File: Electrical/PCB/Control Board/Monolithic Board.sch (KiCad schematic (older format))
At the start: 88 parts, among them J1 ED2627-ND, J10 6posheader, J11 S7038-ND, J12 ED2989-ND-USB, J13 ED1501-ND, J14 ED2989-ND-USB, J15 ED2580-ND, J16 ED2580-ND, J17 ED2744-ND, J18 ED2744-ND, J19 ED2744-ND, J2 ED2627-ND, J20 ED2744-ND, J21 ED2744-ND, J22 ED2744-ND, J23 ED2744-ND, J24 ED2744-ND, J25 ED2744-ND, J26 ED2744-ND, J3 ED2627-ND, J4 ED2627-ND, J5 ED2627-ND, J6 S9175-ND, J7 S9175-ND, J8 6posheader, J9 S7038-ND, M1 Mounting_Holes, T1 test_point, T10 test_point, T11 test_point, T12 test_point, T13 test_point, T14 test_point, T15 test_point, T16 test_point, T17 test_point, T18 test_point, T19 test_point, T2 test_point, T20 test_point, T21 test_point, T3 test_point, T4 test_point, T5 test_point, T6 test_point, T7 test_point, T8 test_point, T9 test_point, U1 LM358-N, U2 LM358-N

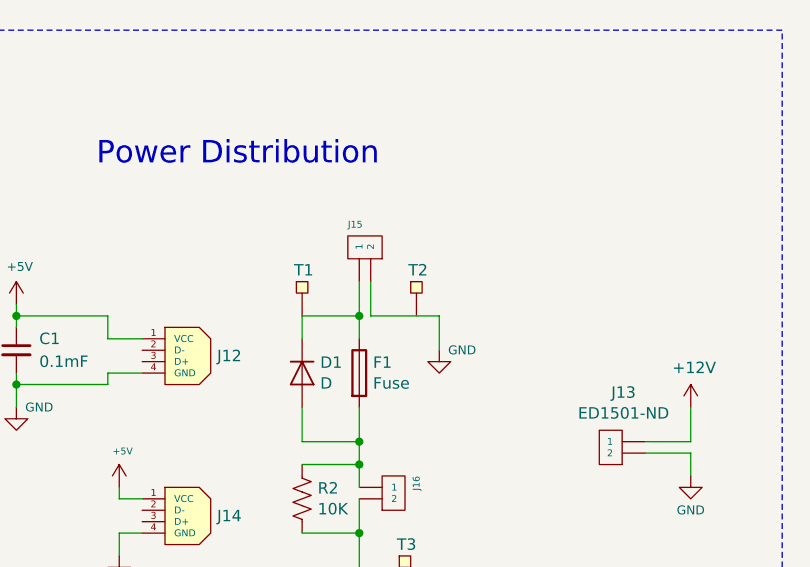
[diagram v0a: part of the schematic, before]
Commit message: Closes #118 by fixing gnd trace for T2 test pad
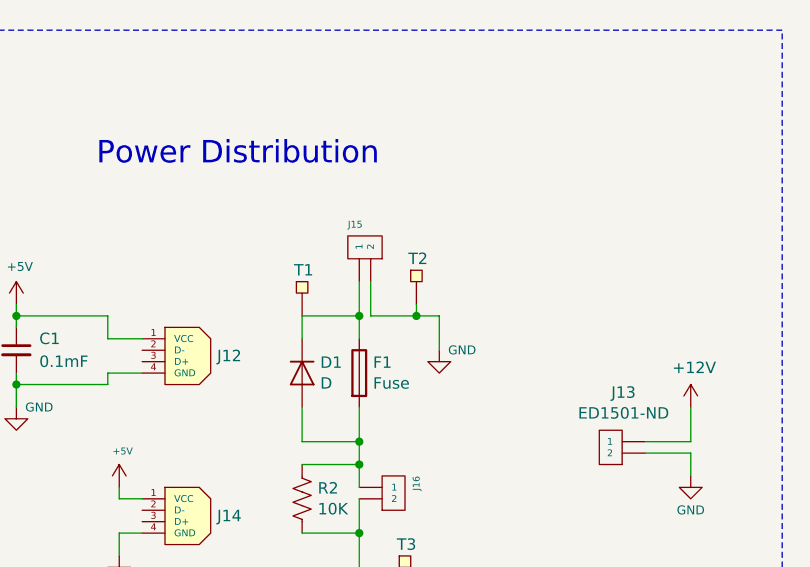
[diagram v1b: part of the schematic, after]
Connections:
- wire segments 458 -> 460
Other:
- moved on the sheet: T2
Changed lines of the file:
@@
 L Monolithic-Board-rescue:test_point-JPL_Robotics_Lib T2
 U 1 1 5C412E03
-P 6150 5950
-F 0 "T2" V 6200 5900 50  0000 L CNN
-F 1 "test_point" H 6300 6200 50  0001 C CNN
-F 2 "TestPoint:TestPoint_Pad_1.0x1.0mm" H 6100 5900 50  0001 C CNN
-F 3 "" H 6100 5900 50  0001 C CNN
-	1    6150 5950
+P 6150 5900
+F 0 "T2" V 6200 5850 50  0000 L CNN
+F 1 "test_point" H 6300 6150 50  0001 C CNN
+F 2 "TestPoint:TestPoint_Pad_1.0x1.0mm" H 6100 5850 50  0001 C CNN
+F 3 "" H 6100 5850 50  0001 C CNN
+	1    6150 5900
 	0    -1   -1   0
 $EndComp
@@
 	13600 7250 14200 7250
 Wire Wire Line
-	5950 6100 6250 6100
+	5950 6100 6150 6100
 Wire Wire Line
 	5900 7300 6150 7300
 Wire Wire Line
 	14200 8150 14600 8150
+Wire Wire Line
+	6150 6050 6150 6100
+Connection ~ 6150 6100
+Wire Wire Line
+	6150 6100 6250 6100
 $EndSCHEMATC
